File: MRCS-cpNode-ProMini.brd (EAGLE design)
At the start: 99.8 x 68.8 mm, 56 parts, among them CON1 0.100, CON2 0.100, CON3 0.100, CON4 0.100, J1 0.100, J2 0.100, J3 2.1mm, P1 CA CC, U1 MAX3465CPD, U2 NE555P

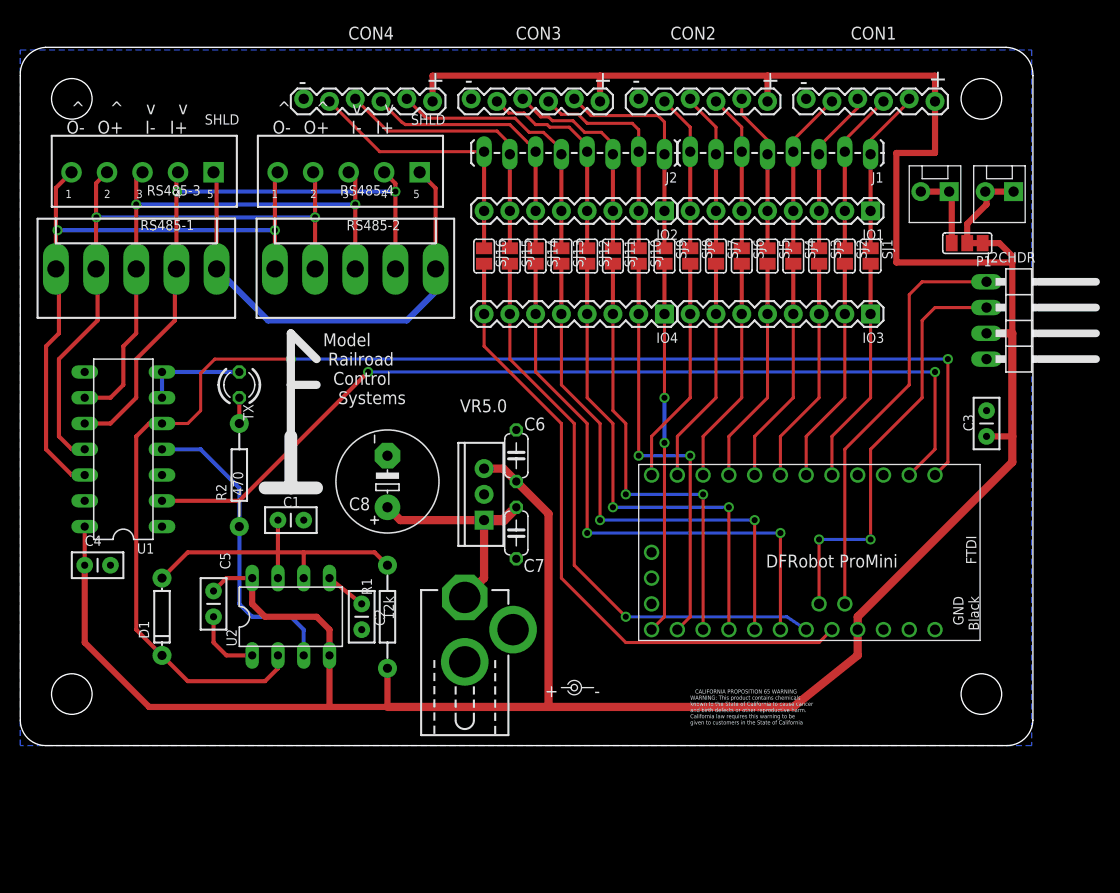
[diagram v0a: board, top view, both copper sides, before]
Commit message: add pullup to pin13
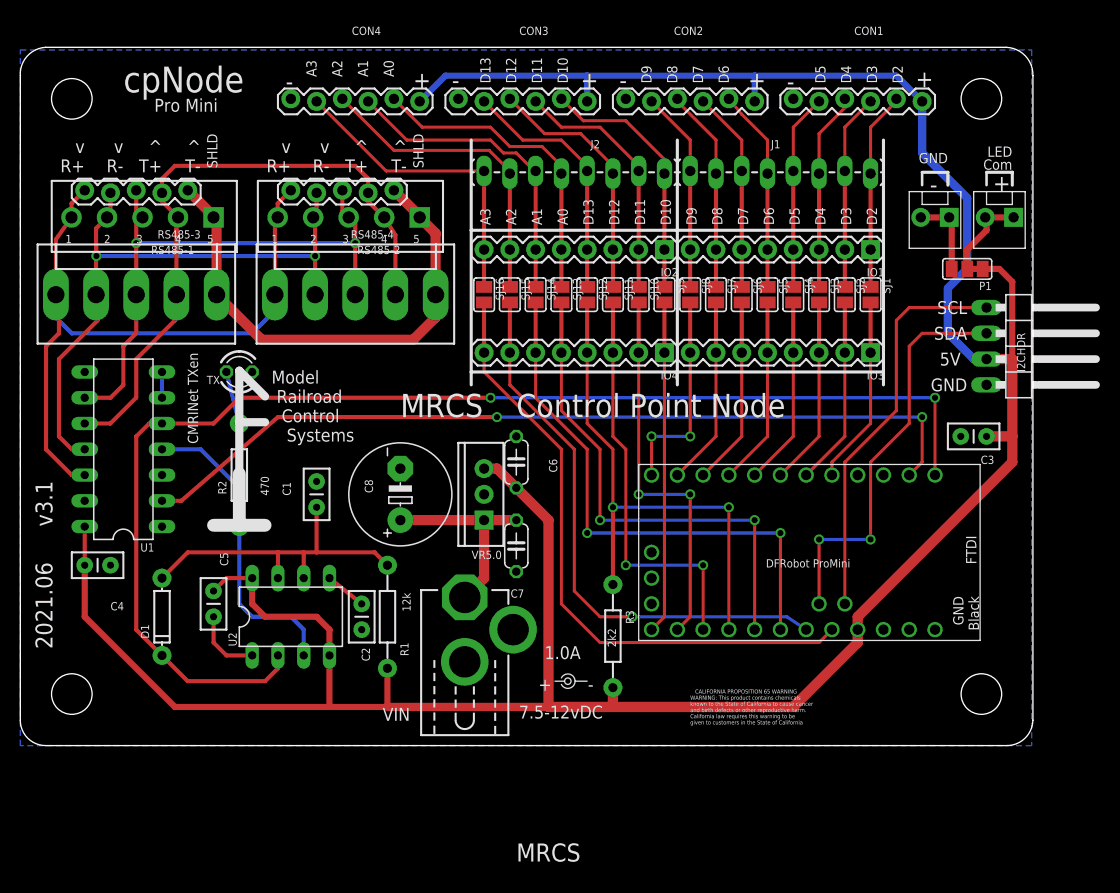
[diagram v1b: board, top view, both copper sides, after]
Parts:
- added CON5, CON6: 0.100, SPCoast:1X05_LOCK
- added R3: 2k2, SPCoast:AXIAL-0.4-RES
- moved U$3 6.27 mm to (21.6, 21.7)
- moved RS485-3 4.45 mm to (11.4, 52.1)
- moved RS485-4 4.45 mm to (31.8, 52.1)
- moved IO3 3.81 mm to (83.8, 38.7)
- moved IO4 3.81 mm to (63.5, 38.7)
- moved IO1 3.81 mm to (83.8, 48.9)
- moved IO2 3.81 mm to (63.5, 48.9)
- moved SJ1 3.81 mm to (83.8, 44.5)
- moved SJ10 3.81 mm to (61.0, 44.5)
- moved SJ11 3.81 mm to (58.4, 44.5)
- moved SJ12 3.81 mm to (55.9, 44.5)
- moved SJ13 3.81 mm to (53.3, 44.5)
- moved SJ14 3.81 mm to (50.8, 44.5)
- moved SJ15 3.81 mm to (48.3, 44.5)
- moved SJ16 3.81 mm to (45.7, 44.5)
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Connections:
- net N$54 renamed TXEN
- net IO12: now also R3.P$1
- net R+: now also CON5.1, CON6.1
- net R-: now also CON5.2, CON6.2
- net SHIELD: now also CON5.5, CON6.5
- net T+: now also CON5.3, CON6.3
- net T-: now also CON5.4, CON6.4
- net VCC: now also R3.P$2
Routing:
- net TX: track 134.2 -> 124.9 mm
- net RX: track 92.7 -> 84.3 mm
- net GND: track 25.0 -> 17.4 mm
- net VCC: track 291.3 -> 284.6 mm
- net R+: track 64.8 -> 70.7 mm, vias 2 -> 0
- net O13: track 27.0 -> 31.7 mm
- net O7: track 15.8 -> 20.1 mm
- net O8: track 15.5 -> 19.9 mm
- net O6: track 15.5 -> 19.9 mm
- net O5: track 15.8 -> 20.1 mm
- net O16: track 26.8 -> 30.8 mm
- net O12: track 20.8 -> 24.7 mm
- net SHIELD: track 46.9 -> 50.8 mm
- net O11: track 21.0 -> 24.8 mm
- net IO12: track 48.6 -> 52.4 mm
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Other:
- board text added: "2021.06"
- board text added: "5V"
- board text added: ">DRAWING_NAME"
- board text added: "CMRINet TXen"
- board text added: "D2"
- board text added: "D3"
- board text added: "MRCS"
- board text added: "Pro Mini"
- board text added: "SCL"
- board text added: "SDA"
- board text added: "v3.1"
- board text removed: "2020.12"
- board text removed: "A4"
- board text removed: "A5"
- board text removed: "MRCS Design"
- board text removed: "v1.0"
- board text removed: "v3.0"
